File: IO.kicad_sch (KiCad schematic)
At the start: 3 parts, among them J1 USB_C_Receptacle_USB2.0_14P

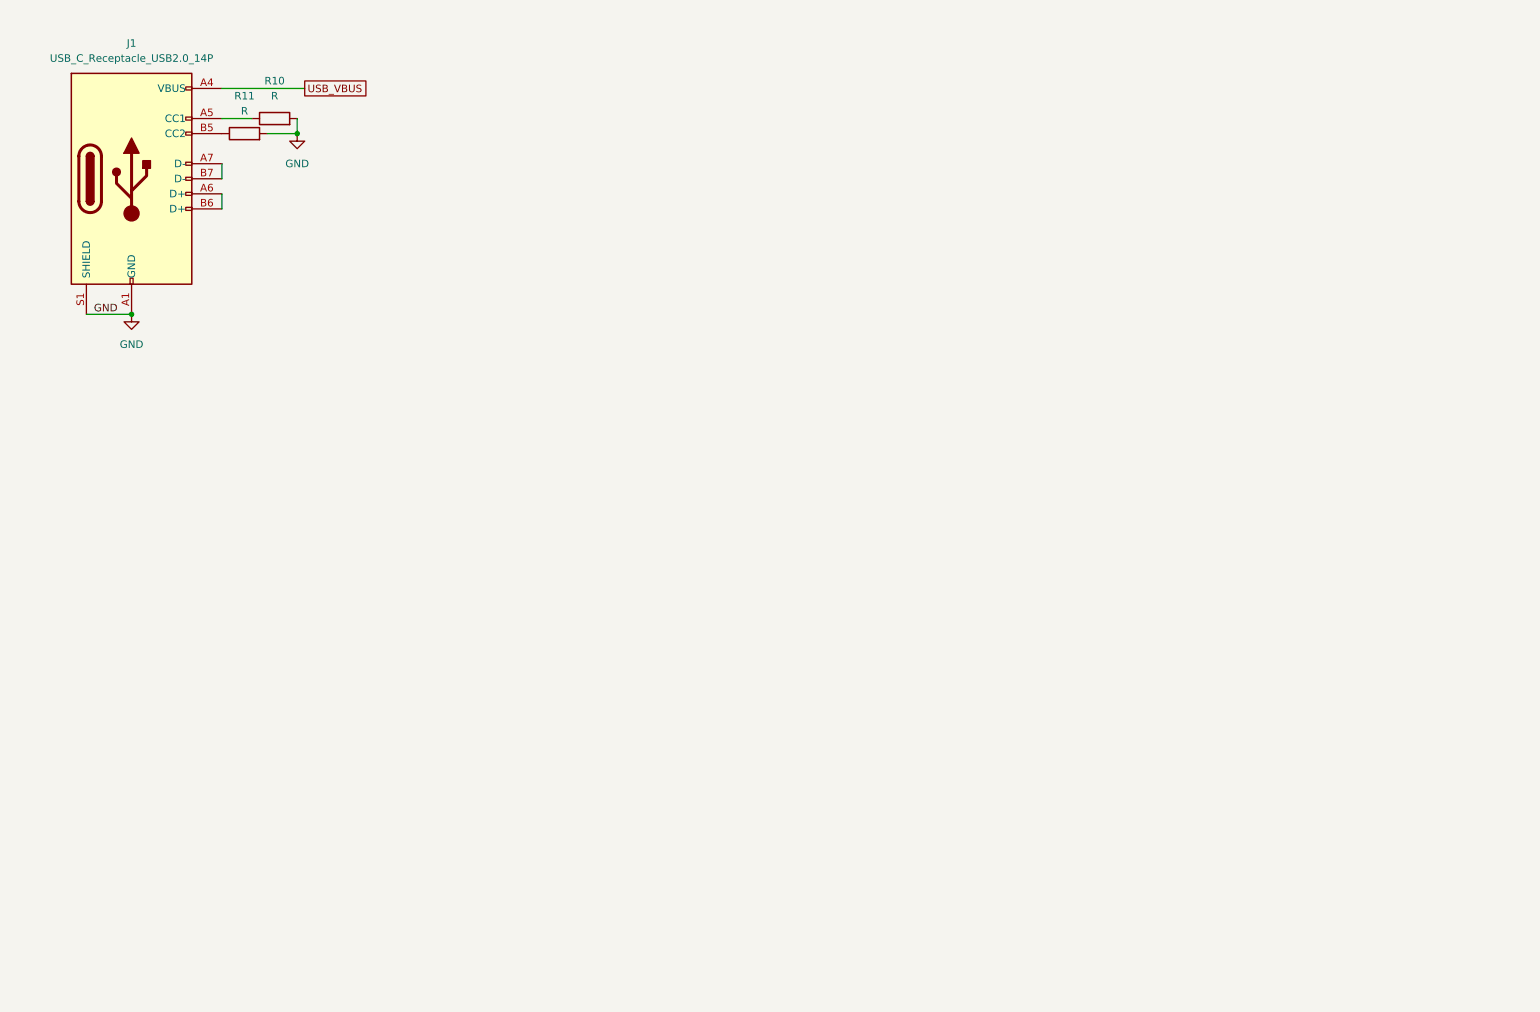
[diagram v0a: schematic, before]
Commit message: Saving before changing RAM from DDR3 to Parallel SDR SRAM
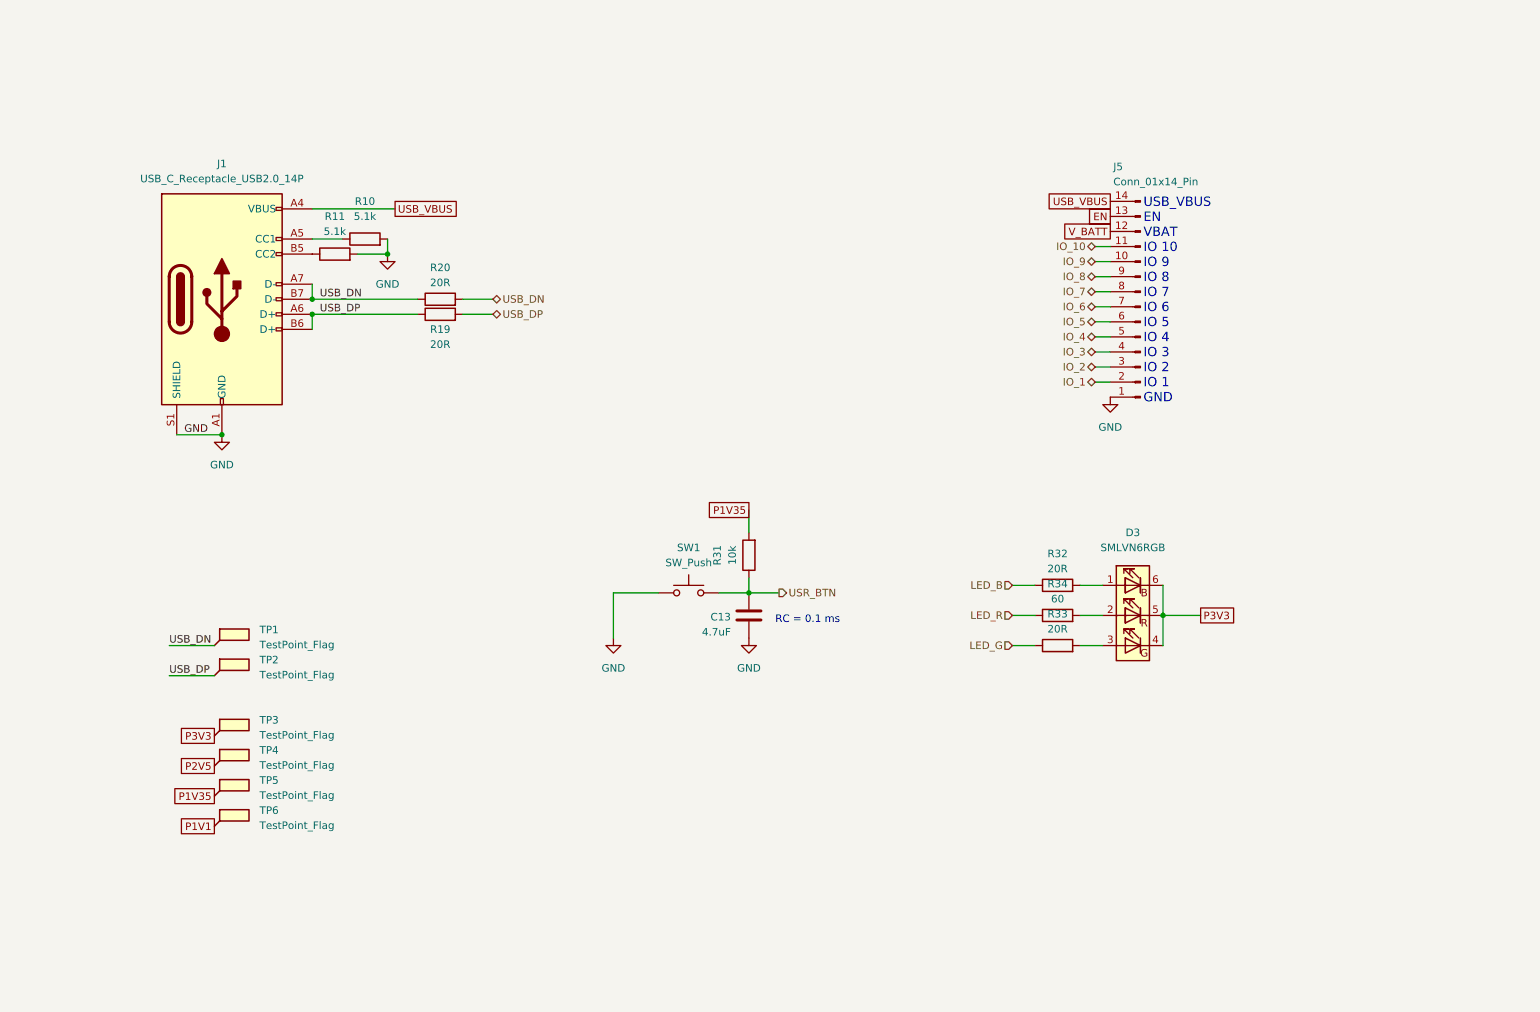
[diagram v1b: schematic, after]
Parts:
- added C13: 4.7uF, symbol Device:C
- added D3: SMLVN6RGB, LED_SMD:LED_ROHM_SMLVN6, symbol LED:SMLVN6RGB
- added J5: Conn_01x14_Pin, symbol Connector:Conn_01x14_Pin
- added R19, R20, R32, R33: 20R, symbol Device:R
- added R31: 10k, symbol Device:R
- added R34: 60, symbol Device:R
- added SW1: SW_Push, symbol Switch:SW_Push
- added TP1, TP2, TP3, TP4, TP5, TP6: TestPoint_Flag, symbol Connector:TestPoint_Flag
- R10, R11: value R -> 5.1k
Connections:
- net GND: now also C13.2, J5.1 (Pin_1), SW1.1
- net USB_VBUS: now also J5.14 (Pin_14)
- net USB_DP: now reaches J1.A6 (D+), J1.B6 (D+)
- net USB_DP: now also R19.1, R19.2, TP2.1
- net USB_DN: now reaches J1.A7 (D-), J1.B7 (D-)
- net USB_DN: now also R20.1, R20.2, TP1.1
- new net: D3.2 (RA), R34.2
- new net: D3.1 (BA), R32.2
- new net: D3.3 (GA), R33.2
- new net EN: J5.13 (Pin_13)
- new net IO_1: J5.2 (Pin_2)
- new net IO_10: J5.11 (Pin_11)
- new net IO_2: J5.3 (Pin_3)
- new net IO_3: J5.4 (Pin_4)
- new net IO_4: J5.5 (Pin_5)
- new net IO_5: J5.6 (Pin_6)
- new net IO_6: J5.7 (Pin_7)
- new net IO_7: J5.8 (Pin_8)
- new net IO_8: J5.9 (Pin_9)
- new net IO_9: J5.10 (Pin_10)
- new net LED_B: R32.1
- new net LED_G: R33.1
- new net LED_R: R34.1
- new net P1V1: TP6.1
- new net P1V35: R31.2, TP5.1
- new net P2V5: TP4.1
- new net P3V3: D3.4 (GK), D3.5 (RK), D3.6 (BK), TP3.1
- new net USR_BTN: C13.1, R31.1, SW1.2
- new net V_BATT: J5.12 (Pin_12)
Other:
- note added: "RC = 0.1 ms"
- note added: "USB_VBUS EN VBAT IO 10 IO 9 IO 8 IO 7 IO 6 IO 5 IO 4 IO 3 IO 2 IO 1 GND"
- moved on the sheet: J1, R10, R11

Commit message: Added more I/O. Changed power regulators
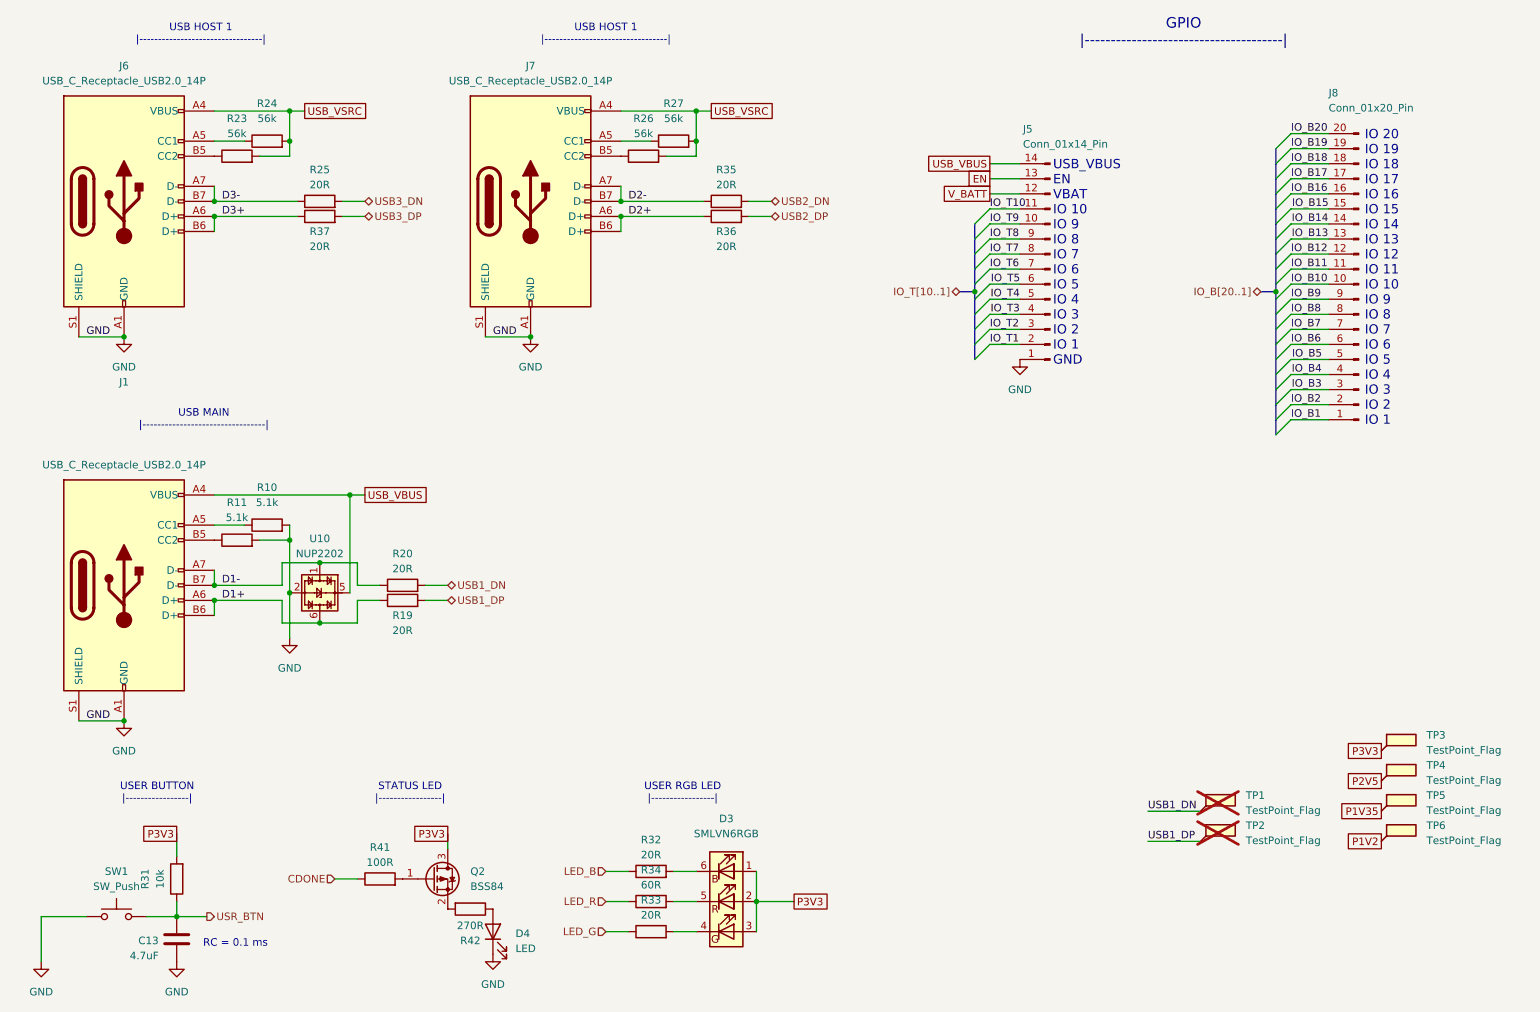
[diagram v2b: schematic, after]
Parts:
- added D4: LED, symbol Device:LED
- added J6, J7: USB_C_Receptacle_USB2.0_14P, symbol Connector:USB_C_Receptacle_USB2.0_14P
- added J8: Conn_01x20_Pin, symbol Connector:Conn_01x20_Pin
- added Q2: BSS84, Package_TO_SOT_SMD:SOT-23, symbol Transistor_FET:BSS84
- added R23, R24, R26, R27: 56k, symbol Device:R
- added R25, R35, R36, R37: 20R, symbol Device:R
- added R41: 100R, symbol Device:R
- added R42: 270R, symbol Device:R
- added U10: NUP2202, Package_TO_SOT_SMD:SOT-363_SC-70-6, symbol Power_Protection:NUP2202
- R34: value 60 -> 60R
- TP1, TP2: now not fitted
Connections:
- net GND: now also D4.1 (K), J6.A1 (GND), J6.A12 (GND), J6.B1 (GND), J6.B12 (GND), J6.S1 (SHIELD), J7.A1 (GND), J7.A12 (GND), J7.B1 (GND), J7.B12 (GND), J7.S1 (SHIELD), U10.2
- net P1V35: no longer R31.2
- net P3V3: now also D3.1 (BA), D3.2 (RA), D3.3 (GA), R31.2, Q2.3 (D); no longer D3.4 (GK), D3.5 (RK), D3.6 (BK)
- net USB_VBUS: now also U10.5
- net at R34.2: now also D3.5 (RK); no longer D3.2 (RA)
- net at R32.2: now also D3.6 (BK); no longer D3.1 (BA)
- net at R33.2: now also D3.4 (GK); no longer D3.3 (GA)
- net IO_1 renamed IO_T1
- net IO_10 renamed IO_T10
- net IO_2 renamed IO_T2
- net IO_3 renamed IO_T3
- net IO_4 renamed IO_T4
- net IO_5 renamed IO_T5
- net IO_6 renamed IO_T6
- net IO_7 renamed IO_T7
- net IO_8 renamed IO_T8
- net IO_9 renamed IO_T9
- net P1V1 renamed P1V2
- net USB_DN renamed D1-
- net D1-: now also U10.1; no longer R20.2, TP1.1
- net USB_DP renamed D1+
- net D1+: now also U10.6; no longer R19.2, TP2.1
- new net: J7.A5 (CC1), R27.1
- new net: J7.B5 (CC2), R26.1
- new net: D4.2 (A), R42.1
- new net: Q2.1 (G), R41.2
- new net: Q2.2 (S), R42.2
- new net: J6.A5 (CC1), R24.1
- new net: J6.B5 (CC2), R23.1
- new net CDONE: R41.1
- new net D2+: J7.A6 (D+), J7.B6 (D+), R36.1
- new net D2-: J7.A7 (D-), J7.B7 (D-), R35.1
- new net D3+: J6.A6 (D+), J6.B6 (D+), R37.1
- new net D3-: J6.A7 (D-), J6.B7 (D-), R25.1
- new net IO_B1: J8.1 (Pin_1)
- new net IO_B10: J8.10 (Pin_10)
- new net IO_B11: J8.11 (Pin_11)
- new net IO_B12: J8.12 (Pin_12)
- new net IO_B13: J8.13 (Pin_13)
- new net IO_B14: J8.14 (Pin_14)
- new net IO_B15: J8.15 (Pin_15)
- new net IO_B16: J8.16 (Pin_16)
- new net IO_B17: J8.17 (Pin_17)
- new net IO_B18: J8.18 (Pin_18)
- new net IO_B19: J8.19 (Pin_19)
- new net IO_B2: J8.2 (Pin_2)
- new net IO_B20: J8.20 (Pin_20)
- new net IO_B3: J8.3 (Pin_3)
- new net IO_B4: J8.4 (Pin_4)
- new net IO_B5: J8.5 (Pin_5)
- new net IO_B6: J8.6 (Pin_6)
- new net IO_B7: J8.7 (Pin_7)
- new net IO_B8: J8.8 (Pin_8)
- new net IO_B9: J8.9 (Pin_9)
- new net USB1_DN: R20.2, TP1.1
- new net USB1_DP: R19.2, TP2.1
- new net USB2_DN: R35.2
- new net USB2_DP: R36.2
- new net USB3_DN: R25.2
- new net USB3_DP: R37.2
- new net USB_VSRC: J6.A4 (VBUS), J6.A9 (VBUS), J6.B4 (VBUS), J6.B9 (VBUS), J7.A4 (VBUS), J7.A9 (VBUS), J7.B4 (VBUS), J7.B9 (VBUS), R23.2, R24.2, R26.2, R27.2
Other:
- note added: "GPIO |--------------------------------------|"
- note added: "IO 20 IO 19 IO 18 IO 17 IO 16 IO 15 IO 14 IO 13 IO 12 IO 11 IO 10 IO 9 IO 8 IO 7 IO 6 IO 5 IO 4 IO 3 IO 2 IO 1"
- note added: "STATUS LED |-----------------|"
- note added: "USB HOST 1 |---------------------------------|"
- note added: "USB MAIN |---------------------------------|"
- note added: "USER BUTTON |-----------------|"
- note added: "USER RGB LED |-----------------|"
- moved on the sheet: C13, D3, J1, J5, R10, R11, R19, R20, R31, R32, R33, R34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

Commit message: Power routed. Saving before reworking ICE40 pins to optimize layout
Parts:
- removed J1, J6, J7: USB_C_Receptacle_USB2.0_14P, symbol Connector:USB_C_Receptacle_USB2.0_14P
- removed J8: Conn_01x20_Pin, symbol Connector:Conn_01x20_Pin
- removed R10, R11: 5.1k, symbol Device:R
- removed R19, R20, R25, R35, R36, R37: 20R, symbol Device:R
- removed R23, R24, R26, R27: 56k, symbol Device:R
- removed TP1, TP2: TestPoint_Flag, symbol Connector:TestPoint_Flag
- removed U10: NUP2202, Package_TO_SOT_SMD:SOT-363_SC-70-6, symbol Power_Protection:NUP2202
- added J8: Conn_01x14_Pin, Connector_PinHeader_2.54mm:PinHeader_1x14_P2.54mm_Vertical, symbol Connector:Conn_01x14_Pin
- added J9: Conn_01x04_Pin, Connector_PinHeader_1.00mm:PinHeader_1x04_P1.00mm_Vertical, symbol Connector:Conn_01x04_Pin
- C13: footprint (none) -> Capacitor_SMD:C_0603_1608Metric
- D4: footprint (none) -> LED_SMD:LED_0603_1608Metric
- J5: footprint (none) -> Connector_PinHeader_2.54mm:PinHeader_1x14_P2.54mm_Vertical
- R31, R32, R33, R34, R41, R42: footprint (none) -> Resistor_SMD:R_0603_1608Metric
- SW1: footprint (none) -> Button_Switch_SMD:SW_SPST_CK_RS282G05A3
- TP1V2: renamed from TP6; footprint (none) -> TestPoint:TestPoint_Keystone_5015_Micro_Mini
- TP2V5: renamed from TP5; footprint (none) -> TestPoint:TestPoint_Keystone_5015_Micro_Mini
- TP3V3: renamed from TP4; footprint (none) -> TestPoint:TestPoint_Keystone_5015_Micro_Mini
- TP5V0: renamed from TP3; footprint (none) -> TestPoint:TestPoint_Keystone_5015_Micro_Mini
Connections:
- net P1V35 is gone; now on net P2V5: TP2V5.1
- net GND: now also J8.1 (Pin_1), J8.12 (Pin_12)
- net IO_B1: now also J8.2 (Pin_2)
- net IO_B10: now also J8.11 (Pin_11)
- net IO_B2: now also J8.3 (Pin_3)
- net IO_B3: now also J8.4 (Pin_4)
- net IO_B4: now also J8.5 (Pin_5)
- net IO_B5: now also J8.6 (Pin_6)
- net IO_B6: now also J8.7 (Pin_7)
- net IO_B7: now also J8.8 (Pin_8)
- net IO_B8: now also J8.9 (Pin_9)
- net IO_B9: now also J8.10 (Pin_10)
- net P2V5: no longer TP3V3.1
- net P3V3: now also TP3V3.1, J8.13 (Pin_13); no longer TP5V0.1
- net USR_BTN renamed USR_BTN1
- net V_BATT renamed USB_VBUS2
- new net EXT_PLL1N: J9.2 (Pin_2)
- new net EXT_PLL1P: J9.1 (Pin_1)
- new net EXT_PLL2N: J9.4 (Pin_4)
- new net EXT_PLL2P: J9.3 (Pin_3)
- new net P5V: TP5V0.1
- new net V_BAT: J8.14 (Pin_14)
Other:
- note added: "USB_VBUS EN P5V IO 10 IO 9 IO 8 IO 7 IO 6 IO 5 IO 4 IO 3 IO 2 IO 1 GND"
- note added: "VBAT 3.3V GND IO 10 IO 9 IO 8 IO 7 IO 6 IO 5 IO 4 IO 3 IO 2 IO 1 GND"
- note removed: "IO 20 IO 19 IO 18 IO 17 IO 16 IO 15 IO 14 IO 13 IO 12 IO 11 IO 10 IO 9 IO 8 IO 7 IO 6 IO 5 IO 4 IO 3 IO 2 IO 1"
- note removed: "USB HOST 1 |---------------------------------|"
- note removed: "USB MAIN |---------------------------------|"
- note removed: "USB_VBUS EN VBAT IO 10 IO 9 IO 8 IO 7 IO 6 IO 5 IO 4 IO 3 IO 2 IO 1 GND"
- moved on the sheet: C13, D3, D4, J5, Q2, R31, R32, R33, R34, R41, R42, SW1

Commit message: Finished board. Added BOM
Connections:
- net P5V is gone; now on net USB_VBUS2: TP5V0.1
- net EXT_PLL1N: now also J9.4 (Pin_4); no longer J9.2 (Pin_2)
- net EXT_PLL1P: now also J9.3 (Pin_3); no longer J9.1 (Pin_1)
- net EXT_PLL2N: now also J9.2 (Pin_2); no longer J9.4 (Pin_4)
- net EXT_PLL2P: now also J9.1 (Pin_1); no longer J9.3 (Pin_3)
